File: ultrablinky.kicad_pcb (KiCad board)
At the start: 2 copper layers, 125 x 135 mm, 121 parts, among them J1 DNP, J2 SJ1-3523N, J3 SJ1-3523N, J4 Barrel_Jack_5.5x2.5, J5 Conn_01x03, J6 Conn_01x03, J7 Terminal5, J8 SJ1-3523N, Q1 DMP6180SK3Q-13, Q2 DMP6180SK3Q-13, Q3 MMBT3904, Q4 MMBT3906, Q5 MMBT3904, Q6 MMBT3904, Q7 IRFZ44ZPBF, SW1 SW_SPDT, SW2 PEC11R-4215F-S0024, SW3 SW_Push, U1 SGTL5000, U2 TPS73618DBV, U3 Teensy4.0, U4 4N25, U5 LM2574HVM-5, U6 MC34071ADR2G, U7 DNP, U8 MCP4706A1T-E/CH, U9 VXO7803-500

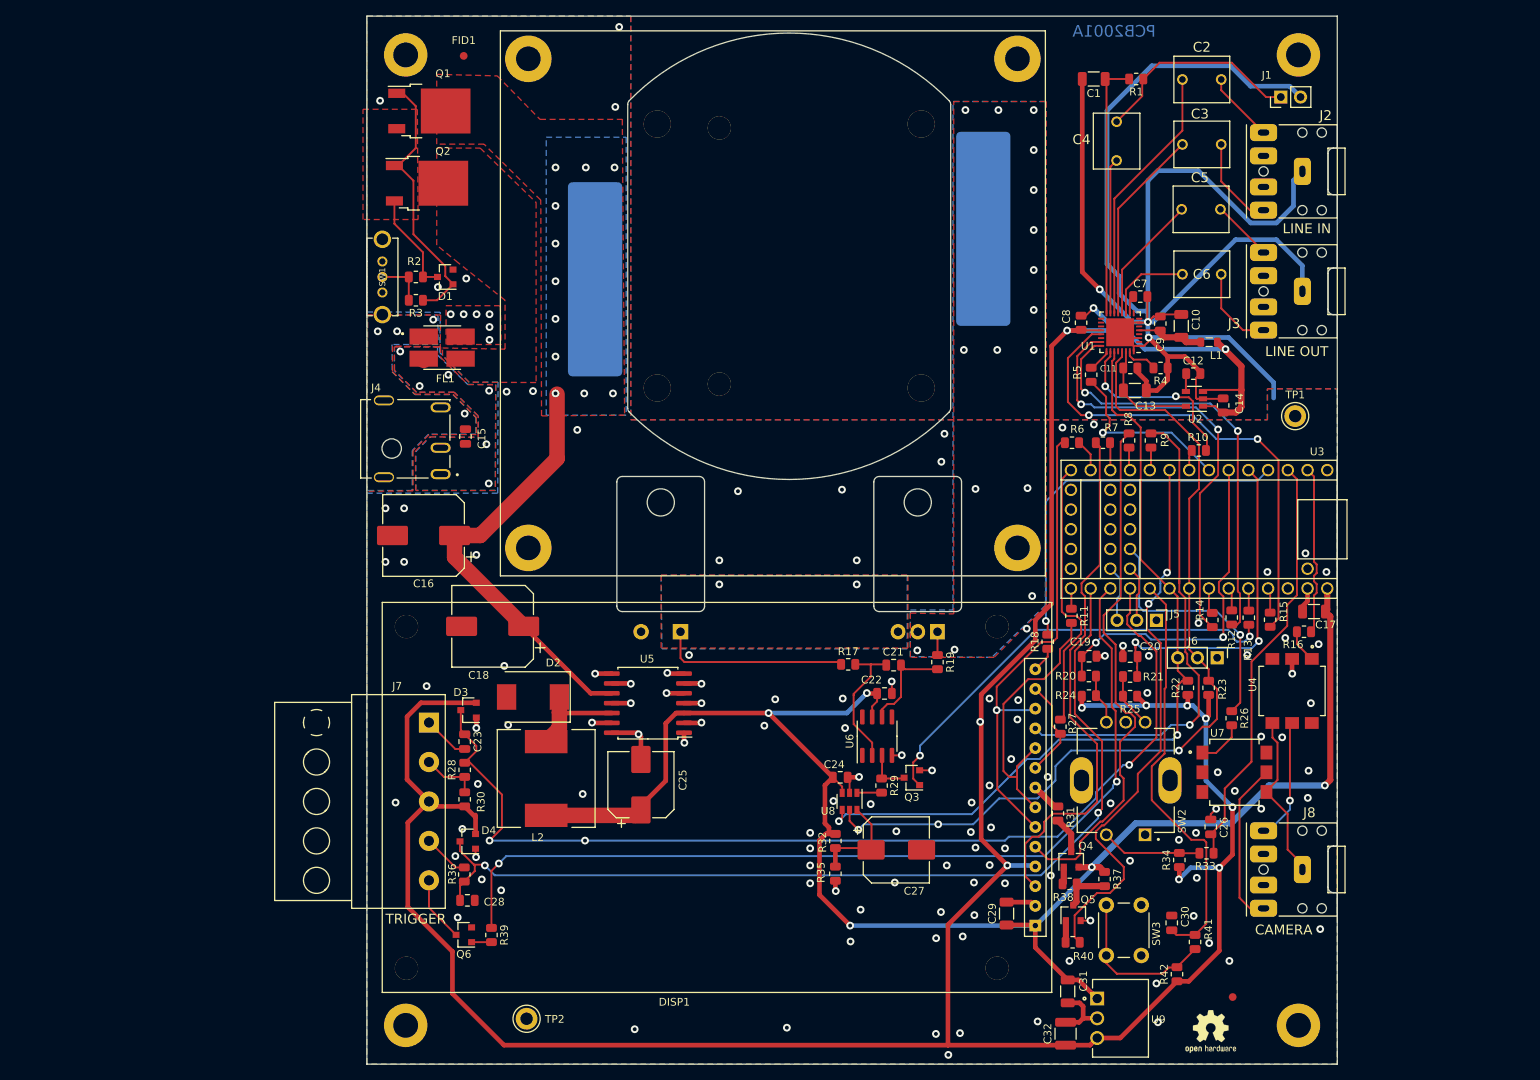
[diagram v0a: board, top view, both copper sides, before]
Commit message: Added Ultrablinky logo symbol and footprint
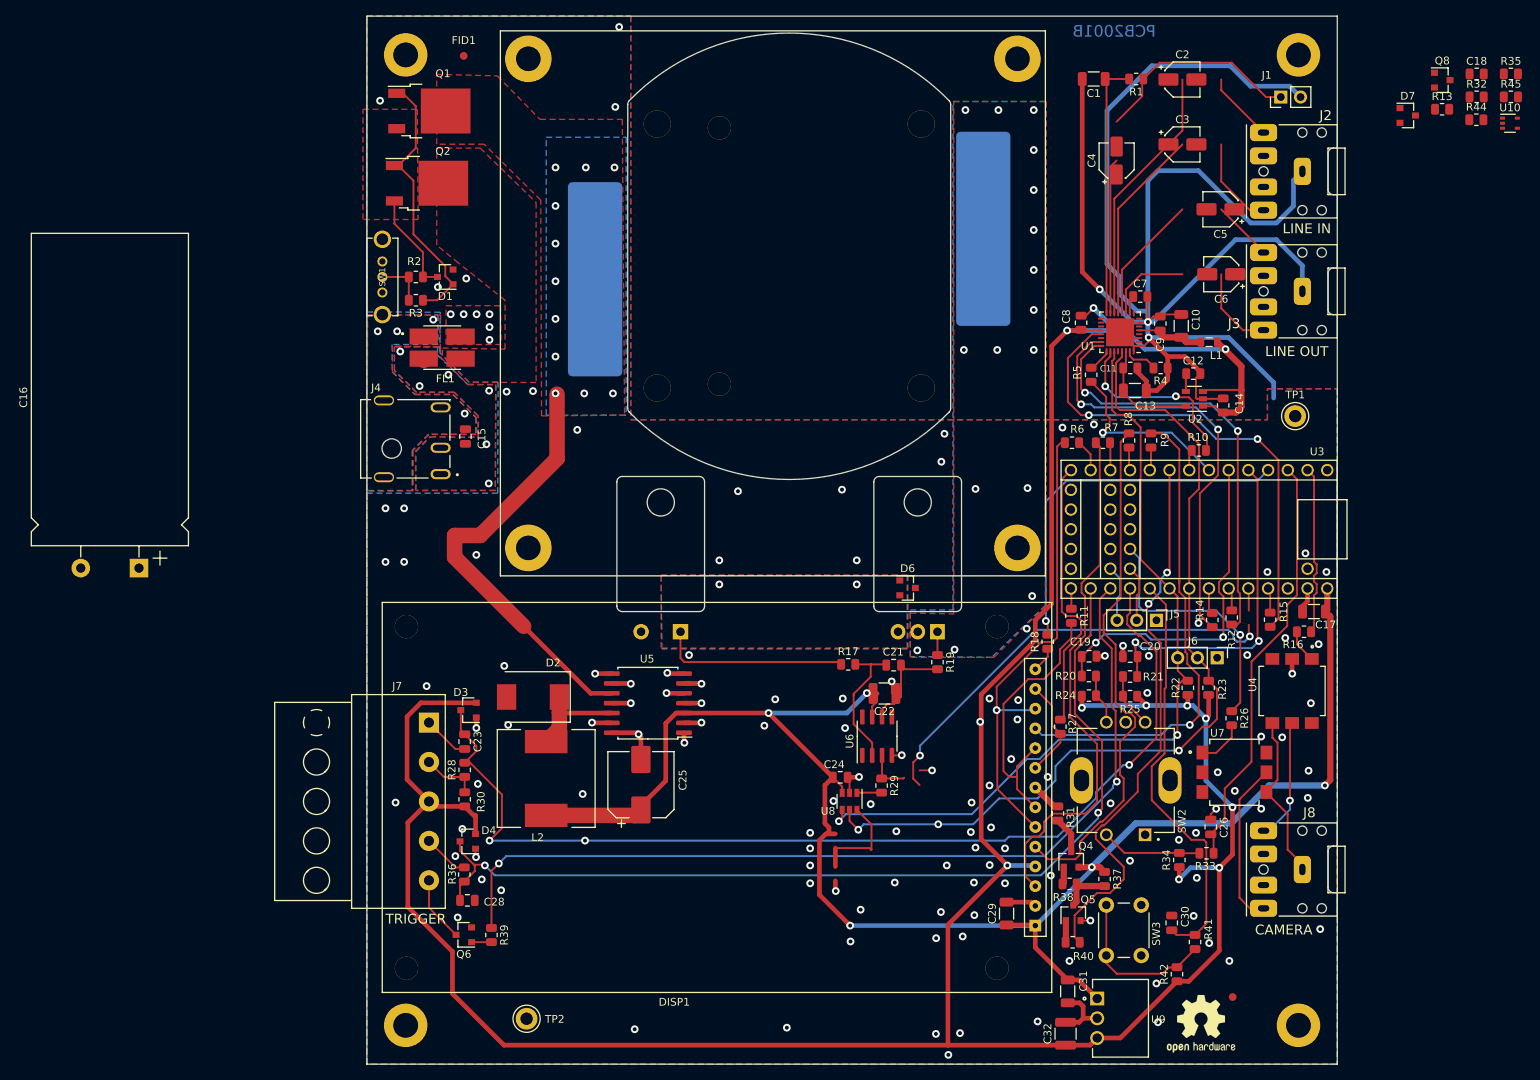
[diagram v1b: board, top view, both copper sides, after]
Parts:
- removed C27: 330uF, Capacitor_SMD:CP_Elec_8x10
- removed Q3: MMBT3904, Package_TO_SOT_SMD:SOT-23
- removed REF**: OSHW-Logo2_7.3x6mm_SilkScreen, Symbol:OSHW-Logo2_7.3x6mm_SilkScreen
- added D6: BZX84C10LT1G, Diode_SMD:D_SOT-23_ANK, F.Cu at (123.3, 102.8)
- added D7: BZX84C27LT1G, Diode_SMD:D_SOT-23_ANK, F.Cu at (187.8, 41.9)
- added LOGO1: Logo_Open_Hardware_Small, Symbol:OSHW-Logo2_9.8x8mm_SilkScreen, F.Cu at (161.2, 158.9)
- added Q8: MMBT3904, Package_TO_SOT_SMD:SOT-23, F.Cu at (192.2, 37.4)
- added R44: 9.76k, Resistor_SMD:R_0805_2012Metric, F.Cu at (196.6, 42.5)
- added R45: 10k, Resistor_SMD:R_0805_2012Metric, F.Cu at (201.1, 39.5)
- added U10: 74VHC1G09, Package_TO_SOT_SMD:SOT-353_SC-70-5, F.Cu at (200.9, 42.9)
- C1: value 10uF -> DNP
- C16: value 82uF -> 3300uF; footprint Capacitor_SMD:CP_Elec_10x10 -> 0_my_footprints:CP_Radial_L40.0mm_D20.0mm_P7.50mm_Horizontal
- C18: value 82uF -> .1uF; footprint Capacitor_SMD:CP_Elec_10x10 -> Resistor_SMD:R_0805_2012Metric
- C2, C3, C5, C6: footprint 0_my_footprints:RSBCC4220Z310K_film_cap -> Capacitor_SMD:CP_Elec_4x5.7
- C21: value 10nF -> 100pF
- C22: value 10nF -> 22uF; footprint Capacitor_SMD:C_0805_2012Metric -> Capacitor_SMD:C_1210_3225Metric
- C4: value 2.2uF -> DNP; footprint 0_my_footprints:RSBCC4220Z310K_film_cap -> Capacitor_SMD:CP_Elec_4x5.7
- J5, J6: value Conn_01x03 -> DNP
- R1: value 2.2k -> DNP
- R13: value 1k -> 33
- R32: value 8.87k -> 22k
- R35: value 4.75k -> 681
- R43: value 0.5 20W -> 0.05 20W
- moved C18 145.4 mm to (196.7, 36.5), turned to 0 degrees
- moved R35 134.8 mm to (201.1, 36.5), turned to 0 degrees
- moved R32 126.5 mm to (196.7, 39.5), turned to 0 degrees
- moved R13 70.1 mm to (192.2, 41.1), turned to 0 degrees
- moved C16 40.6 mm to (20.6, 100.2), turned to 90 degrees
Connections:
- net /V36IN renamed /VIN
- net /V36L renamed /VL
- net /V36SW renamed /VSW
- C16 pad 1: +36V -> VDC
- C18 pad 1: +36V -> VDC
- C22 pad 2: +5V -> Net-(C22-Pad2)
- C5 pad 1: /OUT_L -> /LOUT_L
- C5 pad 2: /LOUT_L -> /OUT_L
- C6 pad 1: /OUT_R -> /LOUT_R
- C6 pad 2: /LOUT_R -> /OUT_R
- D5 pad 2: +36V -> VDC
- Q1 pad 2: +36V -> VDC
- R13 pad 1: Net-(R13-Pad1) -> /PWM
- R13 pad 2: /PWM -> Net-(R13-Pad2)
- R32 pad 1: +5V -> Net-(D7-Pad1)
- R32 pad 2: /V1_5 -> VDC
- R35 pad 1: /V1_5 -> GND
- R35 pad 2: GND -> Net-(C21-Pad2)
- U3 pad 10: Net-(R9-Pad1) -> /I2S_SDIN
- U3 pad 29: Net-(R13-Pad1) -> Net-(R13-Pad2)
- U3 pad 7: /I2S_SDIN -> Net-(R9-Pad1)
- U3 pad 8: Net-(R10-Pad2) -> /D_LEDEN
- U3 pad 9: /D_LEDEN -> Net-(R10-Pad2)
- U5 pad 10: +36V -> VDC
- U6 pad 7: +5V -> Net-(C22-Pad2)
- U8 pad 6: /V1_5 -> Net-(U8-Pad6)
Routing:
- net VDC: track 0.00 -> 55.9 mm, vias 0 -> 11
- net +36V: track 55.9 -> 0.00 mm, vias 11 -> 0
- net Net-(U8-Pad6): track 0.00 -> 13.0 mm
- net /V1_5: track 13.0 -> 0.00 mm
- net Net-(R13-Pad2): track 0.00 -> 2.88 mm
- net Net-(R13-Pad1): track 2.88 -> 0.00 mm
- added copper zone on B.Cu, net VDC
- added copper zone on F.Cu, net VDC
- removed copper zone on B.Cu, net +36V
- removed copper zone on F.Cu, net +36V
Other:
- board text added: "PCB2001B"
- board text removed: "PCB2001A"

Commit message: Updated PCB with schematic changes
The rev B PCB now has the I2S SDIN and I2S SDOUT pins corrected. The
power supply has been changed to 48V. The PWM logic has been inverted.
The bus capacitance has been increased to 3300uF. The capacitors in the
audio path have been changed from film caps to electrolytic. The
Ultrablinky logo has been added.
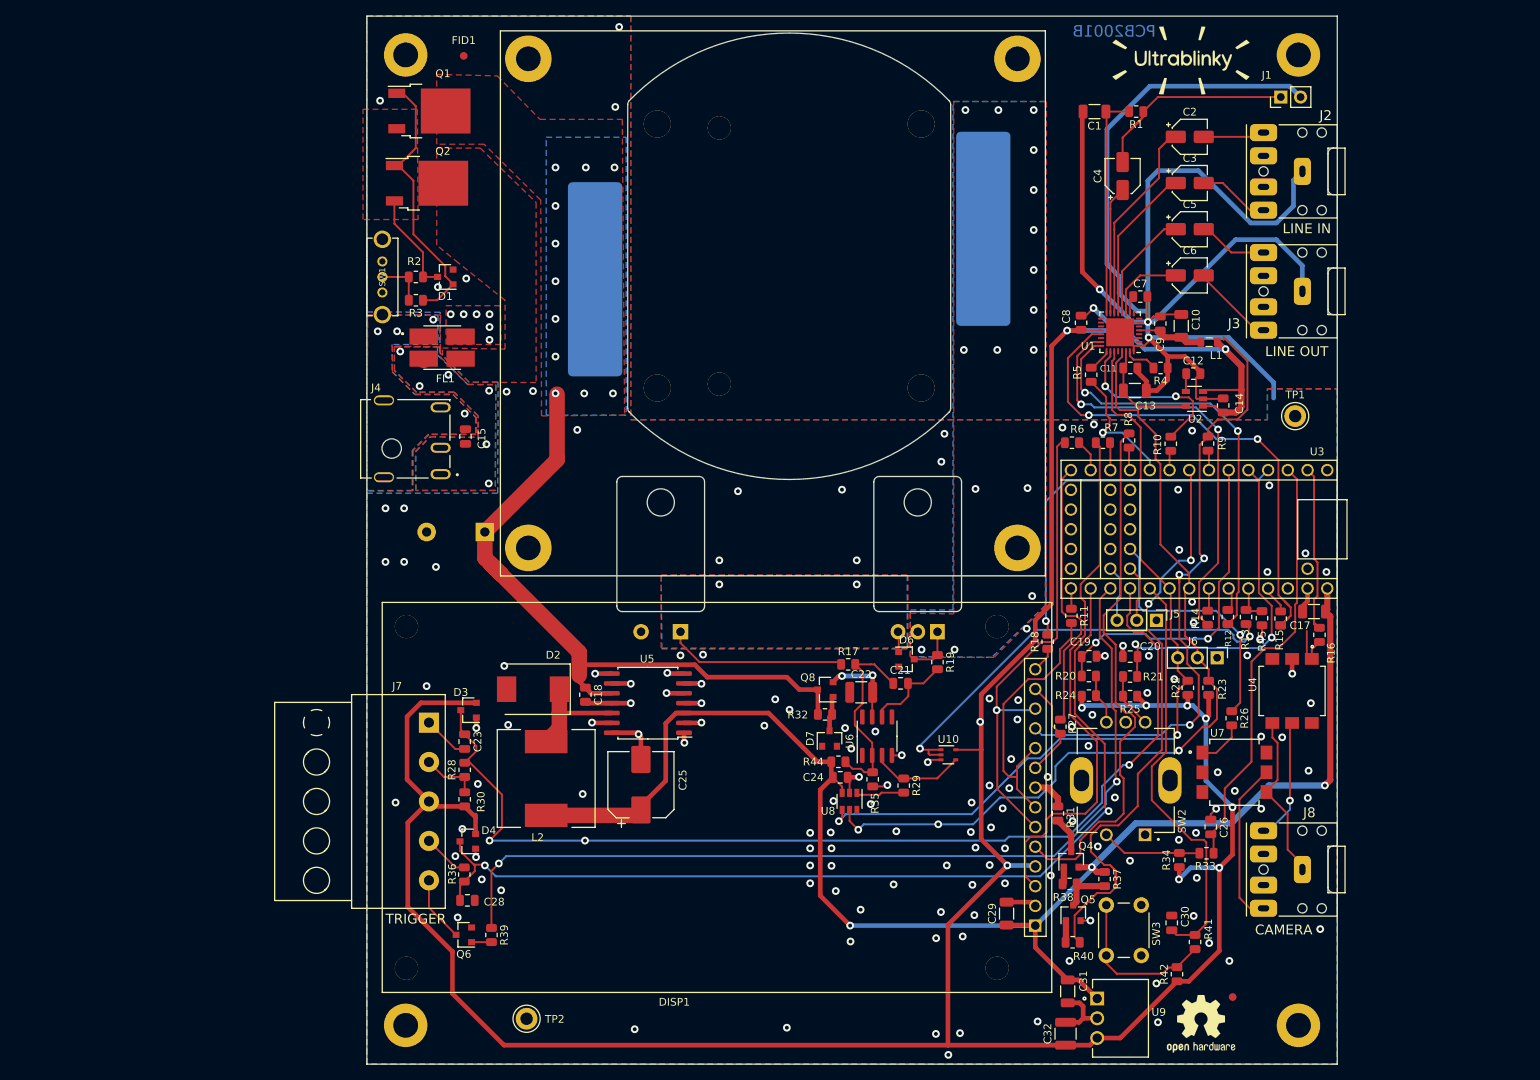
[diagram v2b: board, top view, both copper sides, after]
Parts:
- added LOGO2: Ultrablinky_logo, 0_project_footprints:logo_ultrablinky, F.Cu at (158.6, 34.8)
- C16: moved to B.Cu
- moved C18 139.9 mm to (81.8, 116.5), turned to 270 degrees
- moved R35 122.5 mm to (118.8, 127.4), turned to 90 degrees
- moved R44 116.6 mm to (114.4, 125.2), turned to 180 degrees
- moved R32 115.6 mm to (112.7, 119.0), turned to 180 degrees
- moved Q8 111.7 mm to (112.8, 115.8), turned to 180 degrees
- moved D7 109.5 mm to (113.3, 122.2), turned to 90 degrees
- moved U10 108.9 mm to (128.6, 124.2)
- moved R45 74.4 mm to (169.0, 106.7), turned to 270 degrees
- moved R13 70.1 mm to (166.9, 106.5), turned to 90 degrees
- moved C16 44.8 mm to (65.2, 95.5)
- moved D6 9.20 mm to (123.2, 112.0)
- moved C2 7.45 mm to (159.7, 44.6)
- moved R9 7.36 mm to (162.1, 84.2)
- moved C3 5.06 mm to (159.7, 50.6)
- moved C5 4.71 mm to (159.7, 56.5), turned to 0 degrees
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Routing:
- net VDC: track 55.9 -> 88.0 mm
- net +5V: track 210.0 -> 191.1 mm, vias 5 -> 3
- net /T_CS: track 62.6 -> 80.4 mm, vias 1 -> 3
- net Net-(U8-Pad6): track 13.0 -> 0.00 mm
- net Net-(C22-Pad2): track 0.00 -> 11.0 mm, vias 0 -> 2
- net Net-(C21-Pad2): track 17.7 -> 25.7 mm
- net /LIN_L: track 33.7 -> 26.4 mm
- net /D_LEDEN: track 71.8 -> 78.4 mm
- net /I2S_SDIN: track 23.6 -> 16.9 mm
- net Net-(R29-Pad1): track 5.94 -> 12.2 mm
- net /LIN_R: track 25.2 -> 20.2 mm
- net Net-(D7-Pad1): track 0.00 -> 4.54 mm
- net /BIAS: track 33.3 -> 29.0 mm
- net /SHUTTER: track 21.9 -> 25.7 mm
- net /MIC: track 20.0 -> 16.5 mm
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
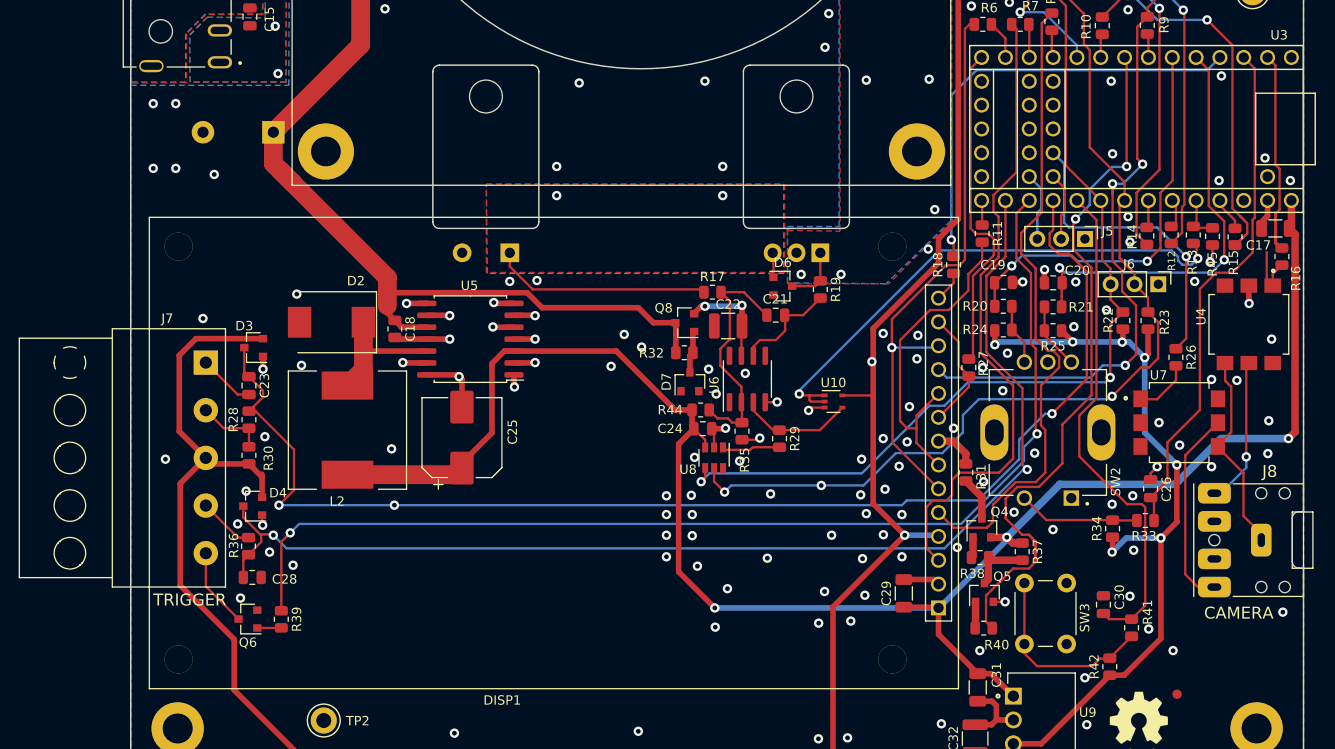
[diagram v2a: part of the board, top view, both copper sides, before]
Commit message: Corrected 4N25 footprints
Previously the 4N25 footprints were too narrow for the pins.
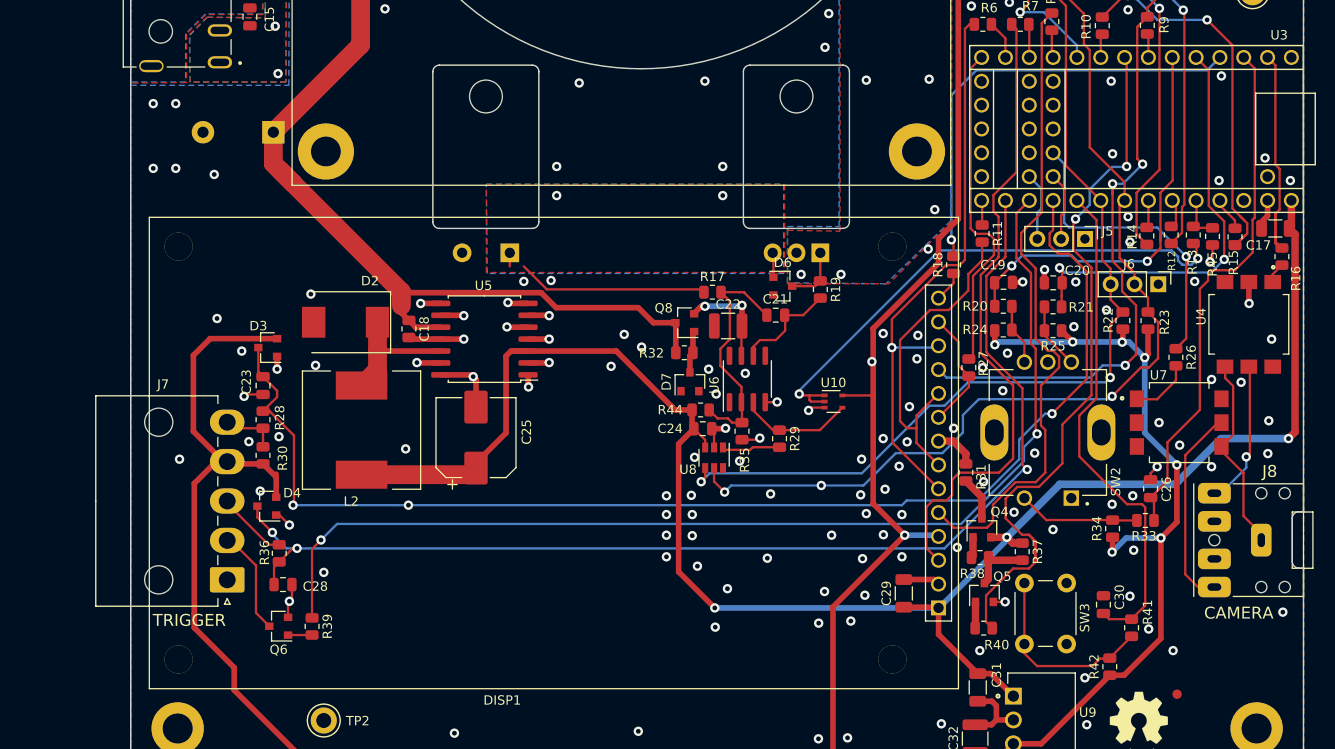
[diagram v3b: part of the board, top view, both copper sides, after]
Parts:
- J7: value Terminal5 -> Conn_01x05; footprint 0_my_footprints:TerminalBlock_Molex_39532-1005,5-5.08_1x05_P5.08mm_Horizontal_Pluggable -> 0_my_footprints:Molex_Mini-Fit_Jr_39-30-3055_1x05_P4.20mm_Horizontal
- moved J7 23.3 mm to (64.0, 143.3), turned to 90 degrees
- moved Q6 3.37 mm to (69.5, 148.2)
- moved R36 3.37 mm to (69.5, 140.4)
- moved R39 3.37 mm to (73.0, 148.2)
- moved C28 3.37 mm to (69.9, 143.8)
- moved C18 1.50 mm to (83.3, 116.5)
- moved C23 1.50 mm to (67.8, 122.5)
- moved C25 1.50 mm to (90.5, 128.1)
- moved D2 1.50 mm to (76.6, 115.8)
- moved D3 1.50 mm to (68.3, 118.5)
- moved D4 1.50 mm to (68.2, 135.4)
- moved L2 1.50 mm to (78.3, 127.3)
- moved R28 1.50 mm to (67.8, 126.2)
- moved R30 1.50 mm to (67.8, 130.0)
- moved U5 1.50 mm to (91.4, 117.6)
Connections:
- J7 pad 2: Net-(J7-Pad2) -> /IR_LED_N
- J7 pad 3: +3V3 -> Net-(J7-Pad3)
- J7 pad 4: Net-(J7-Pad4) -> +3V3
- J7 pad 5: /IR_LED_N -> Net-(J7-Pad5)
- R28 pad 1: Net-(J7-Pad2) -> Net-(J7-Pad5)
- R30 pad 2: Net-(J7-Pad2) -> Net-(J7-Pad5)
- R36 pad 1: Net-(J7-Pad4) -> Net-(J7-Pad3)
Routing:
- net Net-(J7-Pad3): track 0.00 -> 7.62 mm
- net Net-(J7-Pad2): track 7.37 -> 0.00 mm
- net Net-(J7-Pad5): track 0.00 -> 6.06 mm
- net Net-(J7-Pad4): track 5.96 -> 0.00 mm
- net /IRLEDEN: track 119.9 -> 116.9 mm
- net Net-(R16-Pad2): track 6.46 -> 3.50 mm
- net /IR_LED_N: track 8.46 -> 11.2 mm
- net /TRIG_IN_N: track 135.7 -> 133.0 mm
- net /DET_OUT: track 126.3 -> 124.6 mm, vias 2 -> 3
- net /ISENSE: track 25.9 -> 24.4 mm
- net VDC: track 88.0 -> 87.1 mm
- net +3V3: track 384.3 -> 383.7 mm
- net GND: track 311.9 -> 312.4 mm, vias 154 -> 155
